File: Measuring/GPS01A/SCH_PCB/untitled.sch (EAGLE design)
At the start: 43 parts, among them SW1 1.55V, U1 LE33CD-TR, X2 SROUB3M, X3 SROUB3M, X4 SROUB3M, X5 SROUB3M

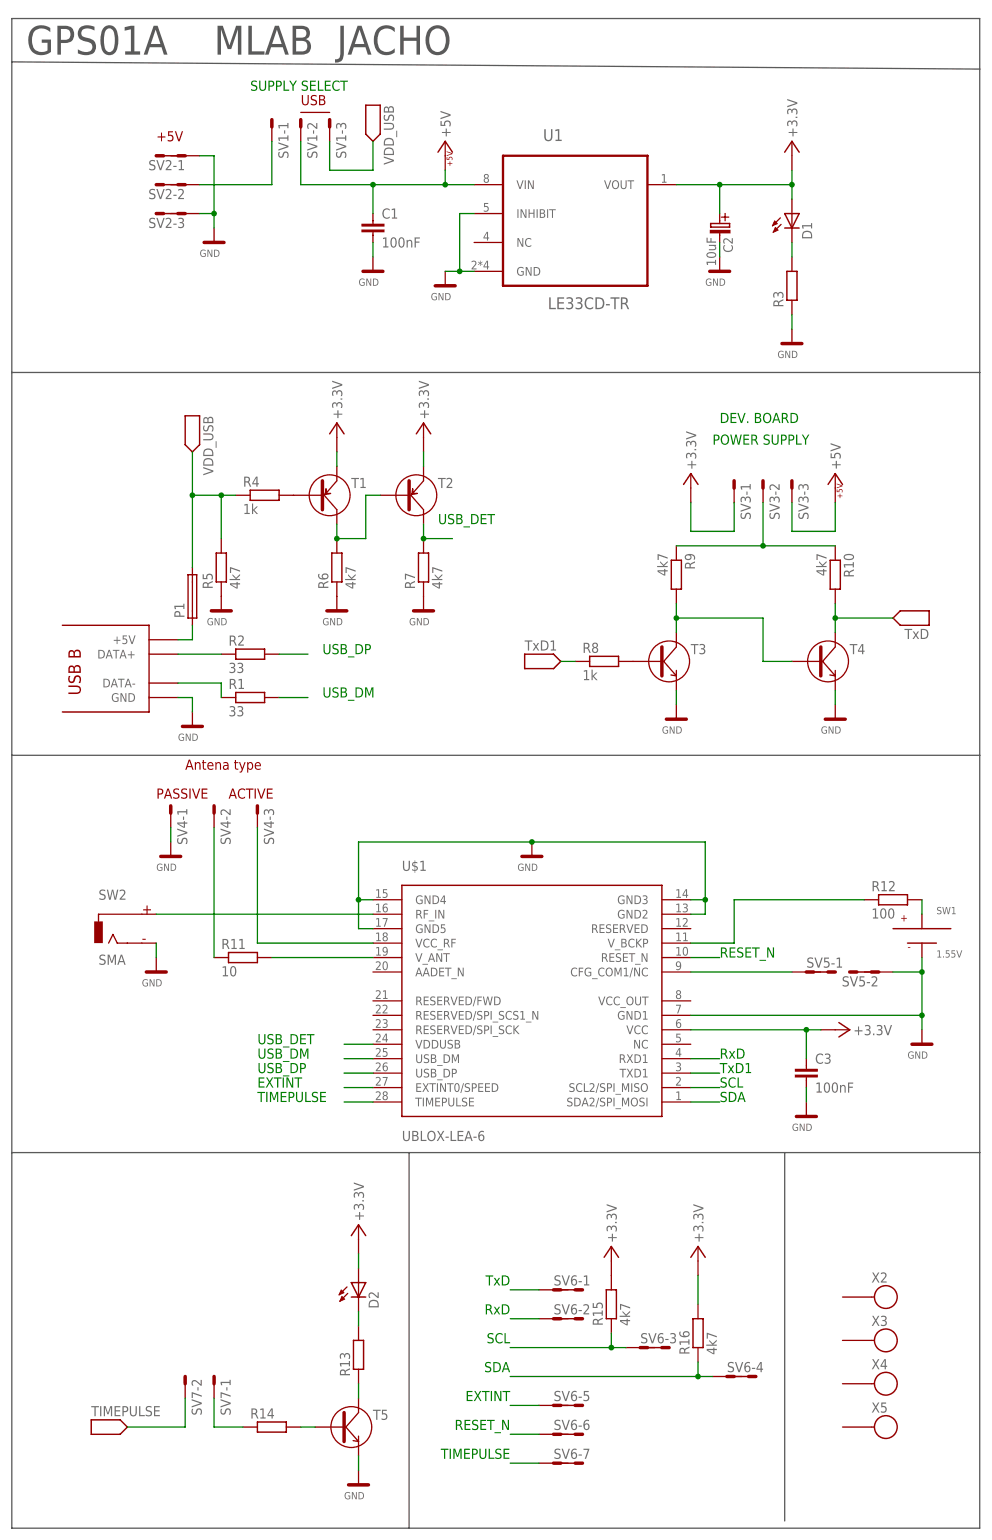
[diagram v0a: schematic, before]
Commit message: 
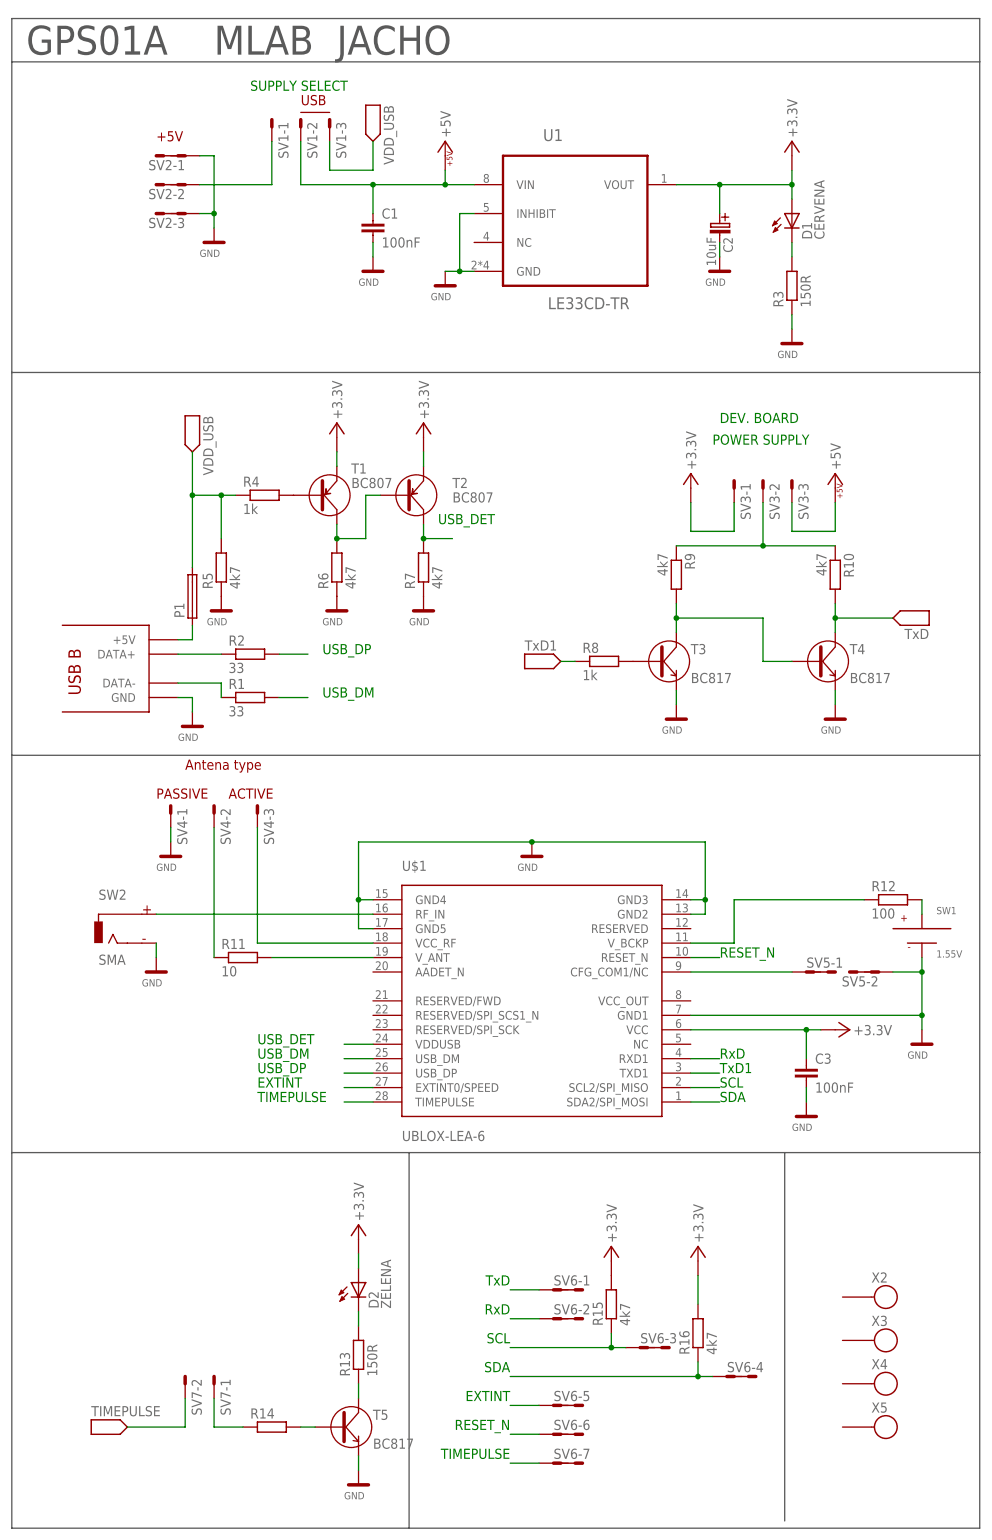
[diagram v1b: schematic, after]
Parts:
- D1: value (none) -> CERVENA
- D2: value (none) -> ZELENA
- R13, R3: value (none) -> 150R
- T1, T2: value (none) -> BC807
- T3, T4, T5: value (none) -> BC817
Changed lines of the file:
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@@
 <setting verticaltext="up"/>
 </settings>
-<grid distance="0.05" unitdist="inch" unit="mm" style="lines" multiple="1" display="no" altdistance="0.01" altunitdist="inch" altunit="inch"/>
+<grid distance="0.1" unitdist="inch" unit="inch" style="lines" multiple="1" display="no" altdistance="0.01" altunitdist="inch" altunit="inch"/>
 <layers>
 <layer number="1" name="Top" color="4" fill="1" visible="no" active="no"/>
@@
 <part name="GND4" library="moje" deviceset="GND" device=""/>
 <part name="GND5" library="moje" deviceset="GND" device=""/>
-<part name="D1" library="moje_diody" deviceset="LED1206" device=""/>
-<part name="R3" library="moje_R" deviceset="R0805" device=""/>
+<part name="D1" library="moje_diody" deviceset="LED1206" device="" value="CERVENA"/>
+<part name="R3" library="moje_R" deviceset="R0805" device="" value="150R"/>
 <part name="GND6" library="moje" deviceset="GND" device=""/>
 <part name="U$4" library="moje_schz" deviceset="+3.3V" device=""/>
-<part name="T1" library="moje_T" deviceset="BC807-16" device=""/>
-<part name="T2" library="moje_T" deviceset="BC807-16" device=""/>
+<part name="T1" library="moje_T" deviceset="BC807-16" device="" value="BC807"/>
+<part name="T2" library="moje_T" deviceset="BC807-16" device="" value="BC807"/>
 <part name="R4" library="moje_R" deviceset="R0805" device="" value="1k"/>
 <part name="R5" library="moje_R" deviceset="R0805" device="" value="4k7"/>
@@
 <part name="U$5" library="moje_schz" deviceset="+3.3V" device=""/>
 <part name="U$6" library="moje_schz" deviceset="+3.3V" device=""/>
-<part name="T3" library="moje_T" deviceset="BC817" device=""/>
-<part name="T4" library="moje_T" deviceset="BC817" device=""/>
+<part name="T3" library="moje_T" deviceset="BC817" device="" value="BC817"/>
+<part name="T4" library="moje_T" deviceset="BC817" device="" value="BC817"/>
 <part name="R8" library="moje_R" deviceset="R0805" device="" value="1k"/>
 <part name="R9" library="moje_R" deviceset="R0805" device="" value="4k7"/>
@@
 <part name="U$12" library="moje_schz" deviceset="+3.3V" device=""/>
 <part name="SV6" library="moje_hrebinky" deviceset="MA07-2" device=""/>
-<part name="D2" library="moje_diody" deviceset="LED1206" device=""/>
-<part name="R13" library="moje_R" deviceset="R0805" device=""/>
-<part name="T5" library="moje_T" deviceset="BC817" device=""/>
+<part name="D2" library="moje_diody" deviceset="LED1206" device="" value="ZELENA"/>
+<part name="R13" library="moje_R" deviceset="R0805" device="" value="150R"/>
+<part name="T5" library="moje_T" deviceset="BC817" device="" value="BC817"/>
 <part name="R14" library="moje_R" deviceset="R0805" device=""/>
 <part name="GND16" library="moje" deviceset="GND" device=""/>
@@
 <wire x1="182.88" y1="-13.97" x2="182.88" y2="55.88" width="0.1524" layer="97"/>
 <wire x1="182.88" y1="55.88" x2="182.88" y2="123.19" width="0.1524" layer="97"/>
-<wire x1="182.88" y1="123.19" x2="182.88" y2="176.53" width="0.1524" layer="97"/>
-<wire x1="182.88" y1="176.53" x2="12.7" y2="177.8" width="0.1524" layer="97"/>
+<wire x1="182.88" y1="123.19" x2="182.88" y2="177.8" width="0.1524" layer="97"/>
+<wire x1="182.88" y1="177.8" x2="12.7" y2="177.8" width="0.1524" layer="97"/>
 <wire x1="182.88" y1="123.19" x2="12.7" y2="123.19" width="0.1524" layer="97"/>
 <wire x1="182.88" y1="55.88" x2="12.7" y2="55.88" width="0.1524" layer="97"/>
@@
 <wire x1="12.7" y1="177.8" x2="12.7" y2="185.42" width="0.1524" layer="97"/>
 <wire x1="12.7" y1="185.42" x2="182.88" y2="185.42" width="0.1524" layer="97"/>
-<wire x1="182.88" y1="185.42" x2="182.88" y2="176.53" width="0.1524" layer="97"/>
+<wire x1="182.88" y1="185.42" x2="182.88" y2="177.8" width="0.1524" layer="97"/>
 <text x="15.24" y="179.07" size="5.08" layer="97">GPS01A</text>
 <text x="48.26" y="179.07" size="5.08" layer="97">MLAB</text>
@@
 <instance part="GND6" gate="G$1" x="149.86" y="130.81"/>
 <instance part="U$4" gate="G$1" x="149.86" y="161.29"/>
-<instance part="T1" gate="A" x="67.31" y="101.6"/>
-<instance part="T2" gate="A" x="82.55" y="101.6"/>
+<instance part="T1" gate="A" x="67.31" y="101.6" smashed="yes">
+<attribute name="NAME" x="72.39" y="105.41" size="1.778" layer="95"/>
+<attribute name="VALUE" x="72.39" y="102.87" size="1.778" layer="96"/>
+</instance>
+<instance part="T2" gate="A" x="82.55" y="101.6" smashed="yes">
+<attribute name="NAME" x="90.17" y="102.87" size="1.778" layer="95"/>
+<attribute name="VALUE" x="90.17" y="100.33" size="1.778" layer="96"/>
+</instance>
 <instance part="R4" gate="G$1" x="57.15" y="101.6"/>
 <instance part="R5" gate="G$1" x="49.53" y="88.9" rot="R90"/>

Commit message: 
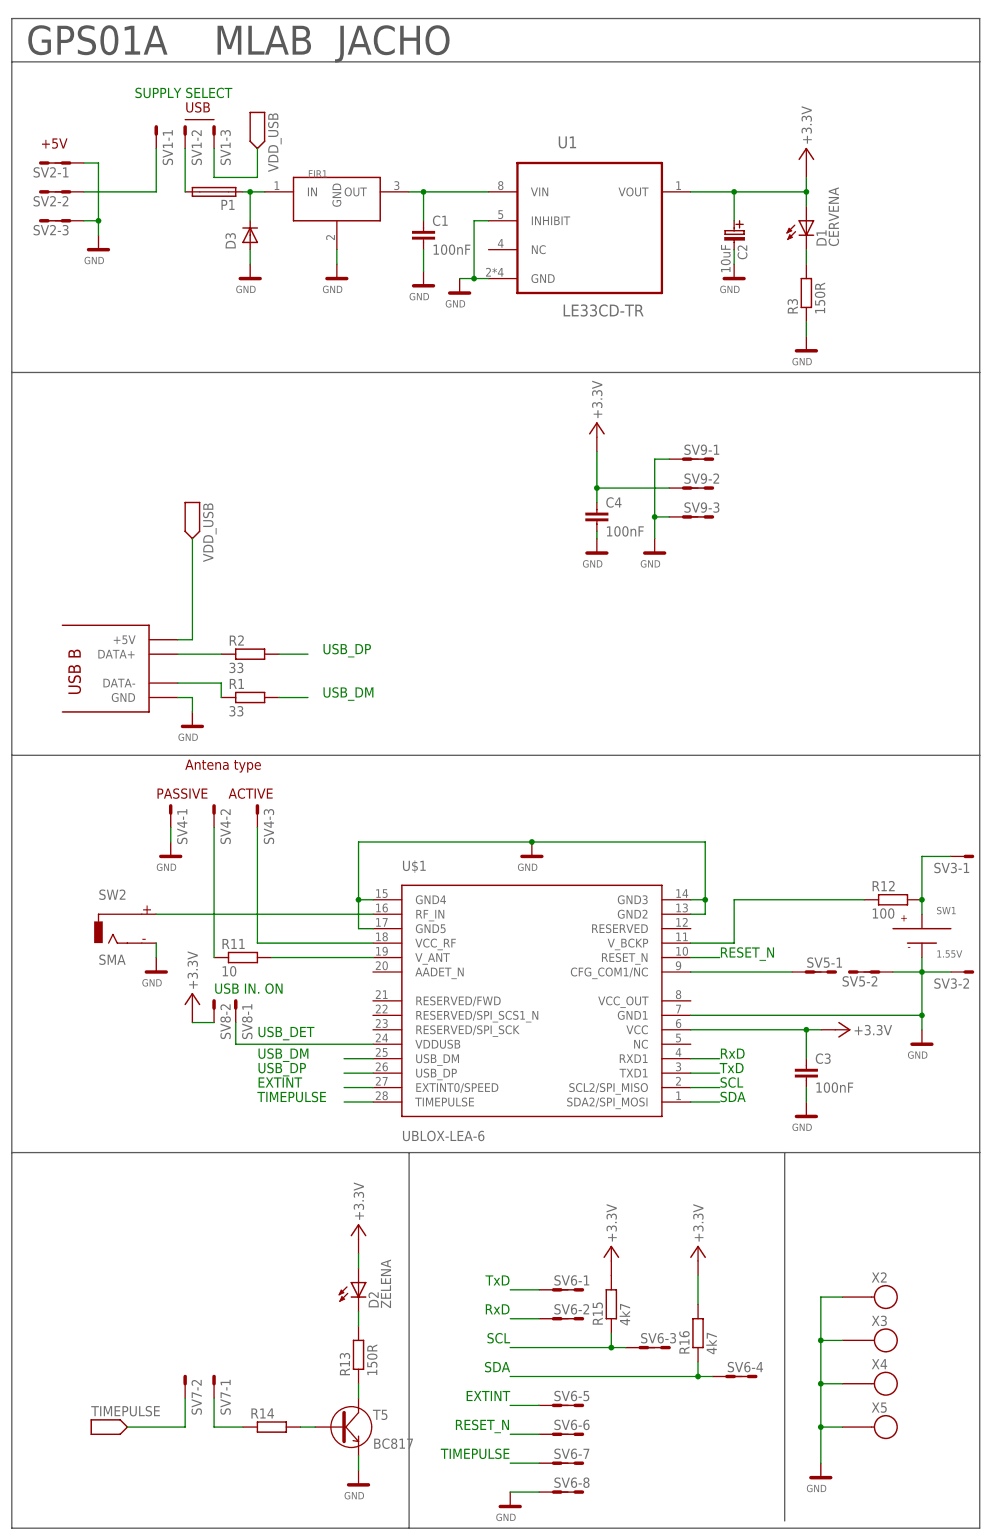
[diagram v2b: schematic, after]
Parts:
- removed R10, R5, R6, R7, R9: 4k7, moje_R:R0805
- removed R4, R8: 1k, moje_R:R0805
- removed T1, T2: BC807, moje_T:BC807-16
- removed T3, T4: BC817, moje_T:BC817
- added C4: 100nF, moje_C:C0805
- added D3: (no value), moje:D-OB.SMA
- added FIR1: (no value), moje:FILTR0805
- added SV8: MA02-1, moje_hrebinky:MA02-1
- added SV9: (no value), moje_hrebinky:MA03-2
- SV3: value (none) -> MA02-1; device moje_hrebinky:MA03-1 -> moje_hrebinky:MA02-1
- SV6: device moje_hrebinky:MA07-2 -> moje_hrebinky:MA08-2
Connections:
- removed net +5V: C1.1, SV1-2.P$1, SV3-3.P$1, U1.VIN
- removed net N$10: R6.2, T1.C, T2.B
- removed net N$6: R8.2, T3.B
- removed net N$8: R4.2, T1.B
- removed net TXD1: R8.1, U$1.TXD1
- net +3.3V: now also C4.1, SV8-2.P$1, SV9-2.K; no longer SV3-1.P$1, T1.E, T2.E
- net GND: now also C4.2, D3.A, FIR1.GND, SV3-2.P$1, SV6-8.K, SV9-1.K, SV9-3.K, X2.P$1, X3.P$1, X4.P$1, X5.P$1; no longer R5.1, R6.1, R7.1, T3.E, T4.E
- net N$12: now also D3.C, FIR1.IN, P1.1; no longer R10.1, R9.1, SV3-2.P$1
- net N$15: now also SV3-1.P$1
- net N$5: now also C1.1, FIR1.OUT, U1.VIN; no longer P1.1, X1.+5V
- net N$7: now also P1.2, SV1-2.P$1; no longer R9.2, T3.C, T4.B
- net TXD: now also U$1.TXD1; no longer R10.2, T4.C
- net USB_DET: now also SV8-1.P$1; no longer R7.2, T2.C
- net VDD_USB: now also X1.+5V; no longer P1.2, R4.1, R5.2
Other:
- note added: "USB IN. ON"
- note removed: "DEV. BOARD"
- note removed: "POWER SUPPLY"
- note removed: "TxD1"
- moved on the sheet: C1, C2, D1, P1, R3, SV1-1, SV1-2, SV1-3, SV2-1, SV2-2, SV2-3, SV3-1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

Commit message: 
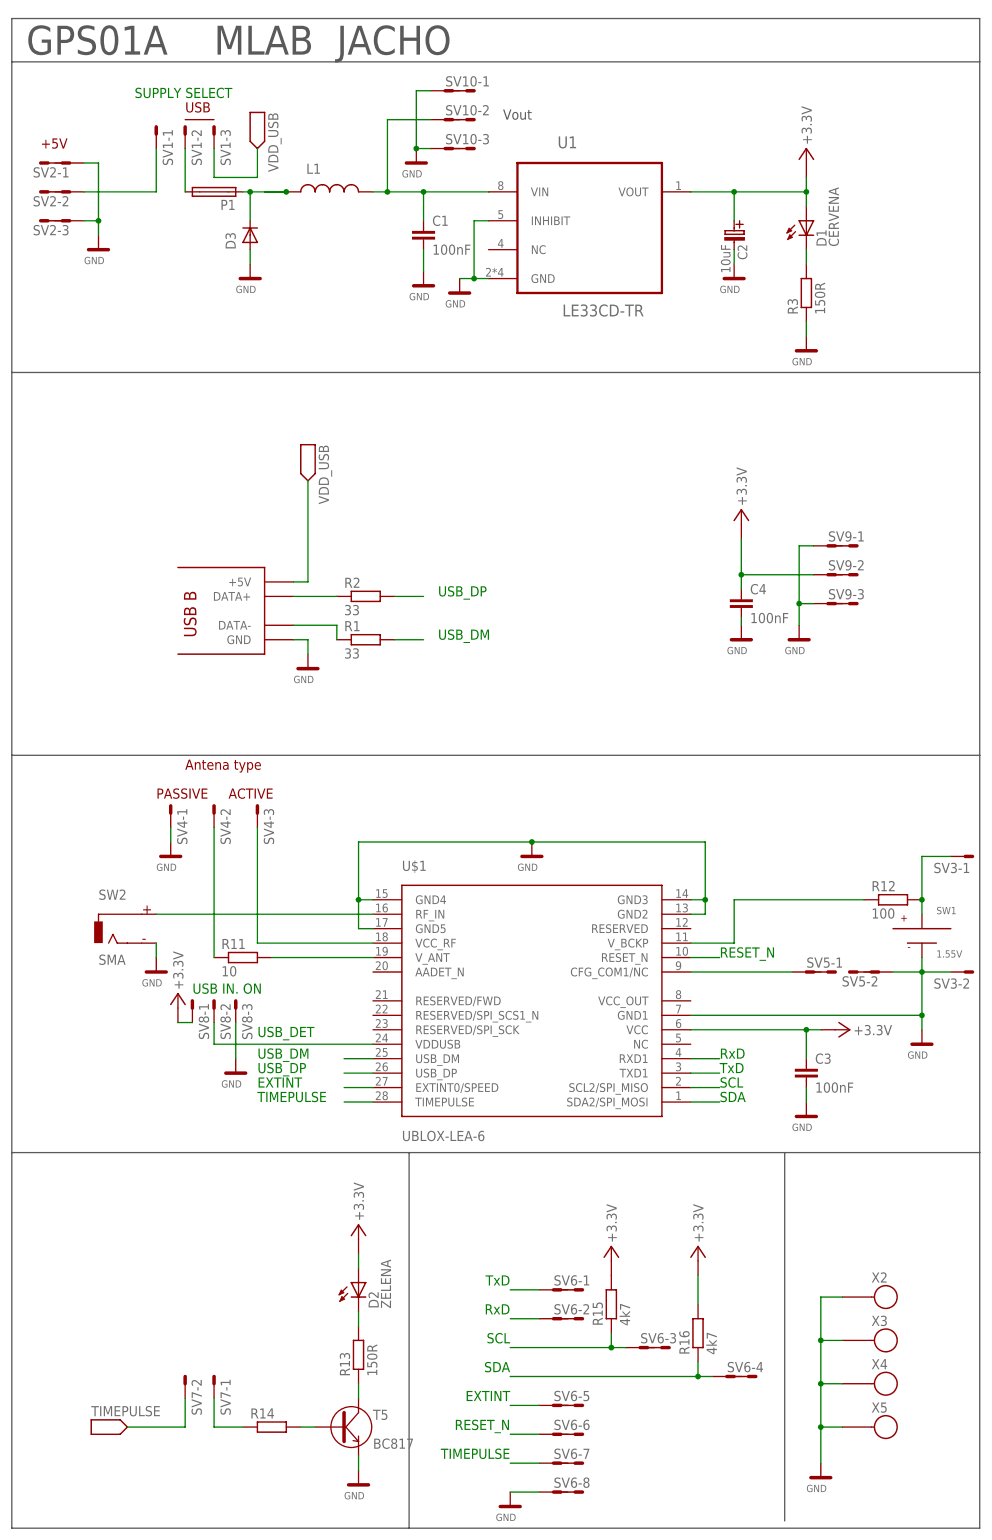
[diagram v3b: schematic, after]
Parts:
- removed FIR1: (no value), moje:FILTR0805
- added L1: (no value), moje_L:L1210
- added SV10: (no value), moje_hrebinky:MA03-2
- SV8: value MA02-1 -> (none); device moje_hrebinky:MA02-1 -> moje_hrebinky:MA03-1
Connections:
- net +3.3V: now also SV8-1.P$1; no longer SV8-2.P$1
- net GND: now also SV10-1.K, SV10-3.K, SV8-3.P$1; no longer FIR1.GND
- net N$12: now also L1.1; no longer FIR1.IN
- net N$5: now also L1.2, SV10-2.K; no longer FIR1.OUT
- net USB_DET: now also SV8-2.P$1; no longer SV8-1.P$1
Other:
- note added: "Vout"
- moved on the sheet: C4, R1, R2, SV8-1, SV9-1, SV9-2, SV9-3
